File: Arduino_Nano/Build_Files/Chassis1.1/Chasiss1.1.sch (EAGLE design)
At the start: 11 parts, among them U2 LM7805

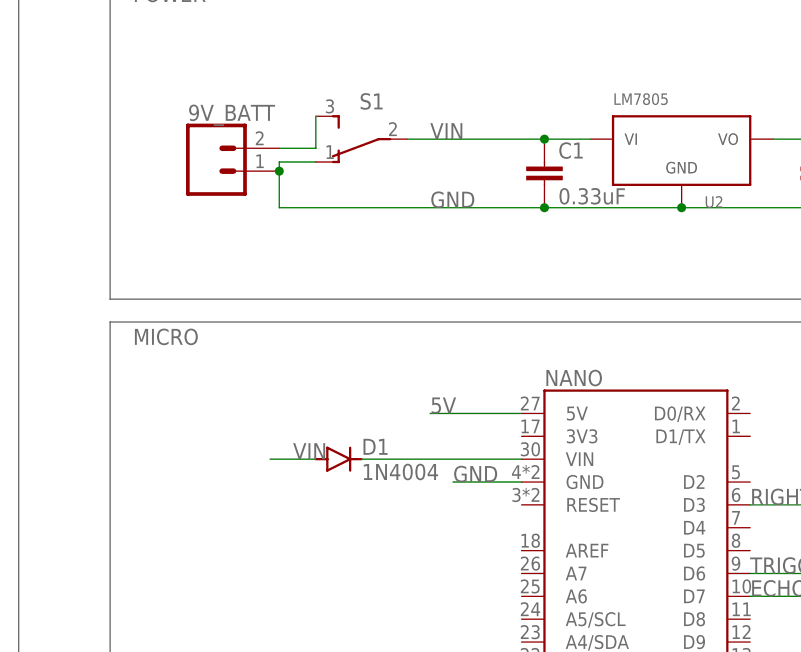
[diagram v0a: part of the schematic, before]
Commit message: Fixed Issue with 3.3v regulator overpowering
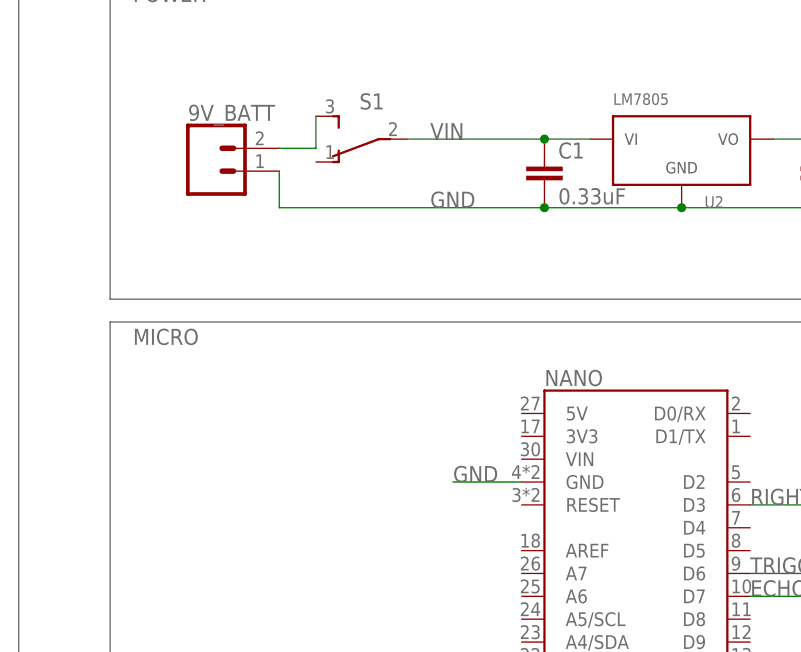
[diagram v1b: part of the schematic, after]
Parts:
- removed D1: 1N4004, diode:1N4004
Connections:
- removed net N$2: D1.C, NANO.VIN
- net 5V: no longer NANO.5V
- net GND: no longer S1.O
- net VIN: no longer D1.A
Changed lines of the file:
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@@
 <part name="9V_BATT" library="SparkFun-Connectors" deviceset="CONN_02" device=""/>
 <part name="S1" library="switch" deviceset="TL36PO" device=""/>
-<part name="D1" library="diode" library_urn="urn:adsk.eagle:library:210" deviceset="1N4004" device="" package3d_urn="urn:adsk.eagle:package:43336/1"/>
 </parts>
 <sheets>
@@
 <attribute name="NAME" x="40.64" y="101.6" size="1.778" layer="95" rot="R180"/>
 </instance>
-<instance part="D1" gate="1" x="35.56" y="60.96" smashed="yes">
-<attribute name="NAME" x="38.1" y="61.4426" size="1.778" layer="95"/>
-<attribute name="VALUE" x="38.1" y="58.6486" size="1.778" layer="96"/>
-</instance>
 </instances>
 <busses>
@@
 <wire x1="139.7" y1="83.82" x2="144.78" y2="83.82" width="0.1524" layer="91"/>
 <label x="142.24" y="83.82" size="1.778" layer="95"/>
-</segment>
-<segment>
-<pinref part="NANO" gate="G$1" pin="5V"/>
-<wire x1="55.88" y1="66.04" x2="45.72" y2="66.04" width="0.1524" layer="91"/>
-<label x="45.72" y="66.04" size="1.778" layer="95"/>
 </segment>
 <segment>
@@
 <pinref part="9V_BATT" gate="G$1" pin="1"/>
 <wire x1="28.956" y1="92.964" x2="28.956" y2="88.9" width="0.1524" layer="91"/>
-<pinref part="S1" gate="BEF1" pin="O"/>
-<wire x1="33.02" y1="93.98" x2="28.956" y2="93.98" width="0.1524" layer="91"/>
-<wire x1="28.956" y1="93.98" x2="28.956" y2="92.964" width="0.1524" layer="91"/>
-<junction x="28.956" y="92.964"/>
 </segment>
 <segment>
@@
 <junction x="58.42" y="96.52"/>
 </segment>
-<segment>
-<pinref part="D1" gate="1" pin="A"/>
-<wire x1="33.02" y1="60.96" x2="27.94" y2="60.96" width="0.1524" layer="91"/>
-<label x="30.48" y="60.96" size="1.778" layer="95"/>
-</segment>
 </net>
 <net name="LEFT_SERVO" class="0">
@@
 <wire x1="33.02" y1="99.06" x2="33.02" y2="95.504" width="0.1524" layer="91"/>
 <wire x1="33.02" y1="95.504" x2="28.956" y2="95.504" width="0.1524" layer="91"/>
-</segment>
-</net>
-<net name="N$2" class="0">
-<segment>
-<pinref part="NANO" gate="G$1" pin="VIN"/>
-<pinref part="D1" gate="1" pin="C"/>
-<wire x1="55.88" y1="60.96" x2="38.1" y2="60.96" width="0.1524" layer="91"/>
 </segment>
 </net>
@@
 </schematic>
 </drawing>
-<compatibility>
-<note version="8.2" severity="warning">
-Since Version 8.2, EAGLE supports online libraries. The ids
-of those online libraries will not be understood (or retained)
-with this version.
-</note>
-<note version="8.3" severity="warning">
-Since Version 8.3, EAGLE supports URNs for individual library
-assets (packages, symbols, and devices). The URNs of those assets
-will not be understood (or retained) with this version.
-</note>
-<note version="8.3" severity="warning">
-Since Version 8.3, EAGLE supports the association of 3D packages
-with devices in libraries, schematics, and board files. Those 3D
-packages will not be understood (or retained) with this version.
-</note>
-</compatibility>
 </eagle>

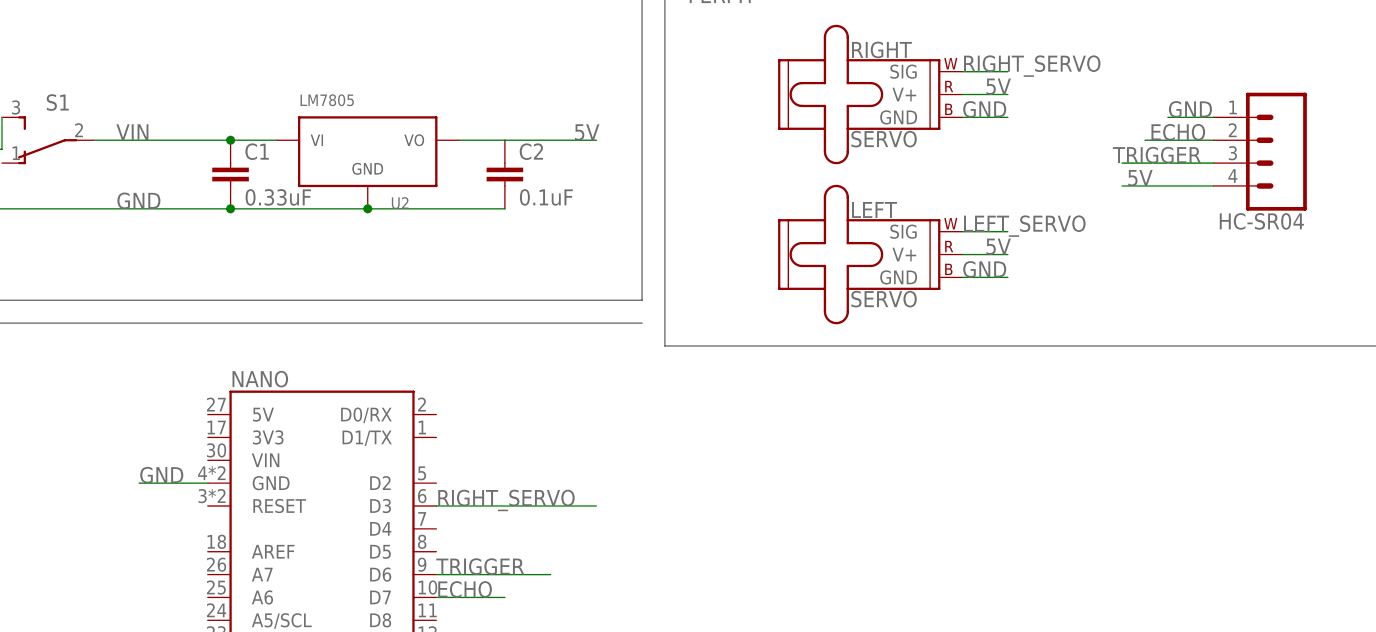
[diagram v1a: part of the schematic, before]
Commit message: Reverse diode not needed, routing was done incorrectly by accident. Also added route from voltage regulator to the Arduino Nano for power. Updated some notes in the README and cleaned out some unused files.
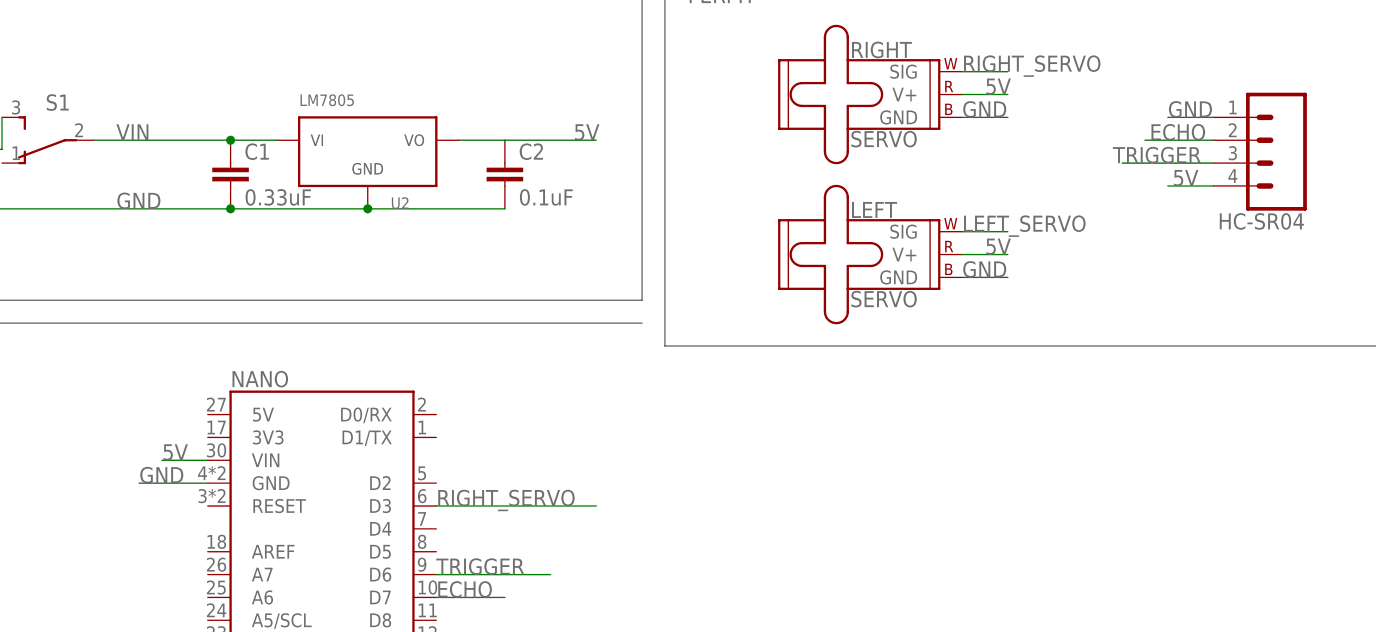
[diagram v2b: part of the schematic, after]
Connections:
- net 5V: now also NANO.VIN
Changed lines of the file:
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@@
 <setting verticaltext="up"/>
 </settings>
-<grid distance="0.1" unitdist="inch" unit="inch" style="lines" multiple="1" display="no" altdistance="0.01" altunitdist="inch" altunit="inch"/>
+<grid distance="0.1" unitdist="inch" unit="inch" style="lines" multiple="1" display="yes" altdistance="0.01" altunitdist="inch" altunit="inch"/>
 <layers>
 <layer number="1" name="Top" color="4" fill="1" visible="no" active="no"/>
@@
 <segment>
 <pinref part="HC-SR04" gate="J1" pin="4"/>
-<wire x1="167.64" y1="91.44" x2="157.48" y2="91.44" width="0.1524" layer="91"/>
-<label x="157.988" y="91.44" size="1.778" layer="95"/>
+<wire x1="167.64" y1="91.44" x2="162.56" y2="91.44" width="0.1524" layer="91"/>
+<label x="163.068" y="91.44" size="1.778" layer="95"/>
+</segment>
+<segment>
+<pinref part="NANO" gate="G$1" pin="VIN"/>
+<wire x1="50.8" y1="60.96" x2="55.88" y2="60.96" width="0.1524" layer="91"/>
+<label x="50.8" y="60.96" size="1.778" layer="95"/>
 </segment>
 </net>

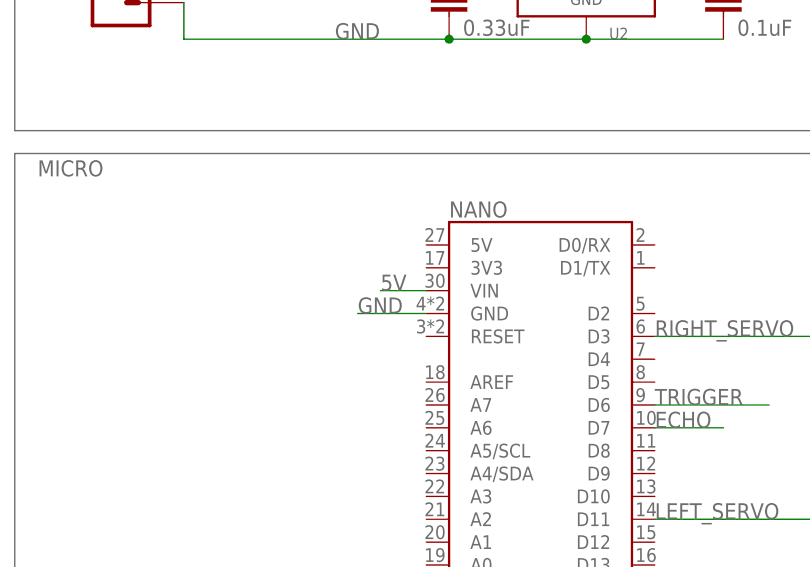
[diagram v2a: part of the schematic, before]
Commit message: fix to power Arduino board
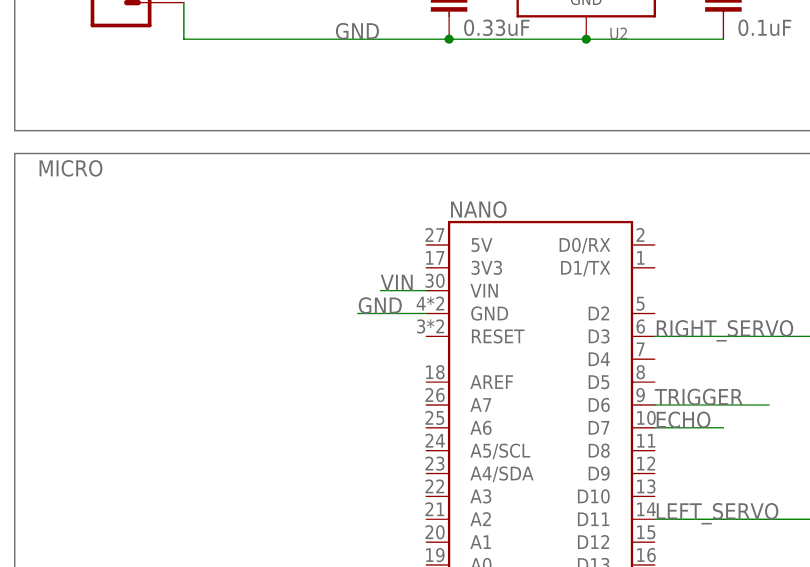
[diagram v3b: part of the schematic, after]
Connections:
- net 5V: no longer NANO.VIN
- net VIN: now also NANO.VIN
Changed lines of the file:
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@@
 <label x="163.068" y="91.44" size="1.778" layer="95"/>
-</segment>
-<segment>
-<pinref part="NANO" gate="G$1" pin="VIN"/>
-<wire x1="50.8" y1="60.96" x2="55.88" y2="60.96" width="0.1524" layer="91"/>
-<label x="50.8" y="60.96" size="1.778" layer="95"/>
 </segment>
 </net>
@@
 <junction x="58.42" y="96.52"/>
 </segment>
+<segment>
+<pinref part="NANO" gate="G$1" pin="VIN"/>
+<wire x1="50.8" y1="60.96" x2="55.88" y2="60.96" width="0.1524" layer="91"/>
+<label x="50.8" y="60.96" size="1.778" layer="95"/>
+</segment>
 </net>
